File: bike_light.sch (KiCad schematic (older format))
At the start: 0 parts

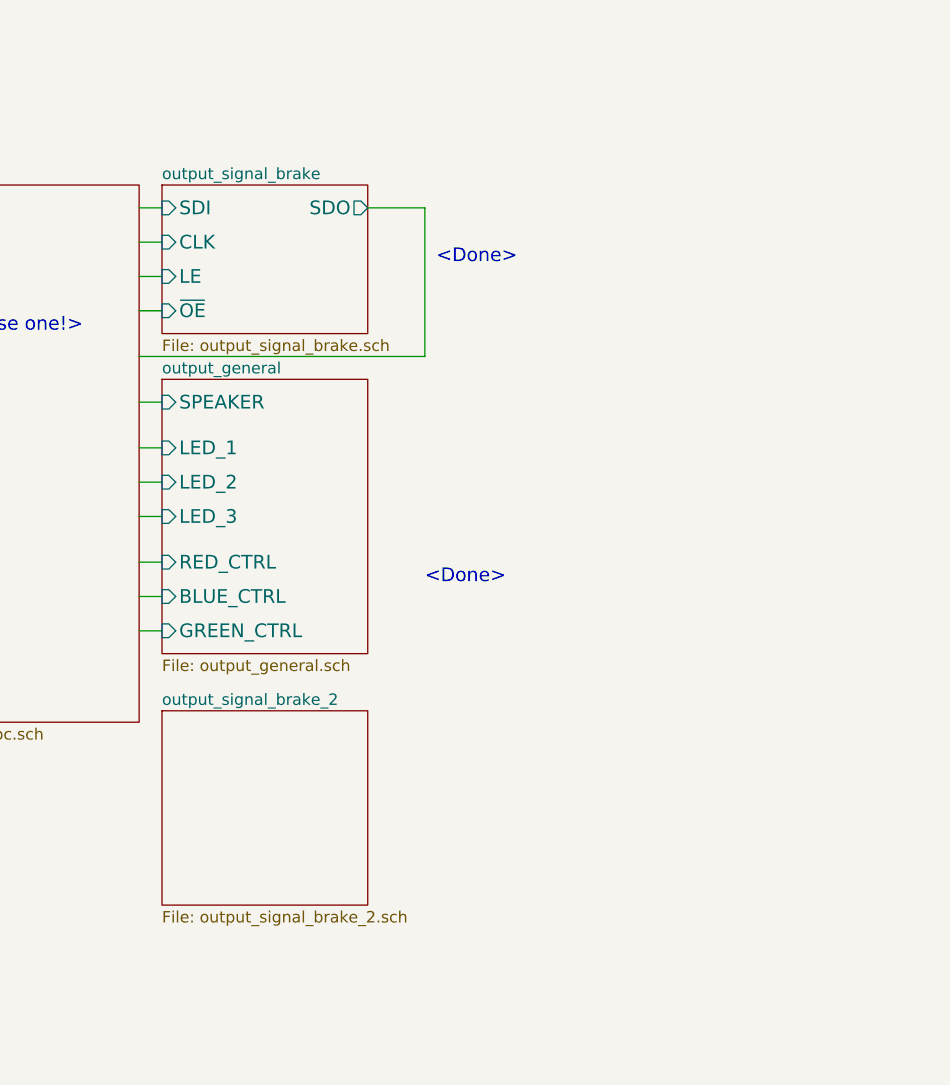
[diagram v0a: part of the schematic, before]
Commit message: finished batt-current LED driver array over I2C
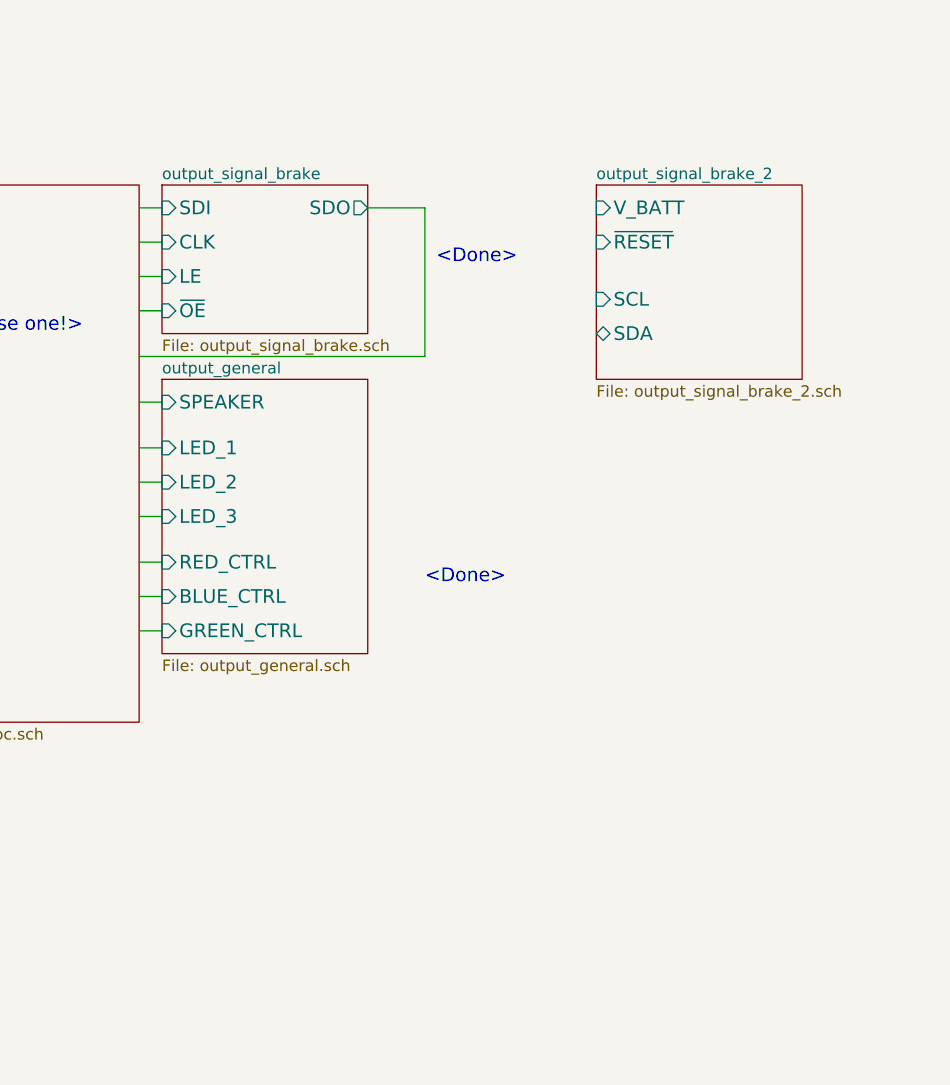
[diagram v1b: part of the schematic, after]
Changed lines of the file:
@@
 Sheet 1 16
 Title "Bike Light"
-Date "5 dec 2013"
+Date "6 dec 2013"
 Rev "1.0"
 Comp ""
@@
 $EndSheet
 $Sheet
-S 6700 4050 900  850
+S 8600 1750 900  850
 U 52A0B607
 F0 "output_signal_brake_2" 50
 F1 "output_signal_brake_2.sch" 50
+F2 "V_BATT" I L 8600 1850 60
+F3 "SCL" I L 8600 2250 60
+F4 "SDA" B L 8600 2400 60
+F5 "~RESET" I L 8600 2000 60
 $EndSheet
 $EndSCHEMATC

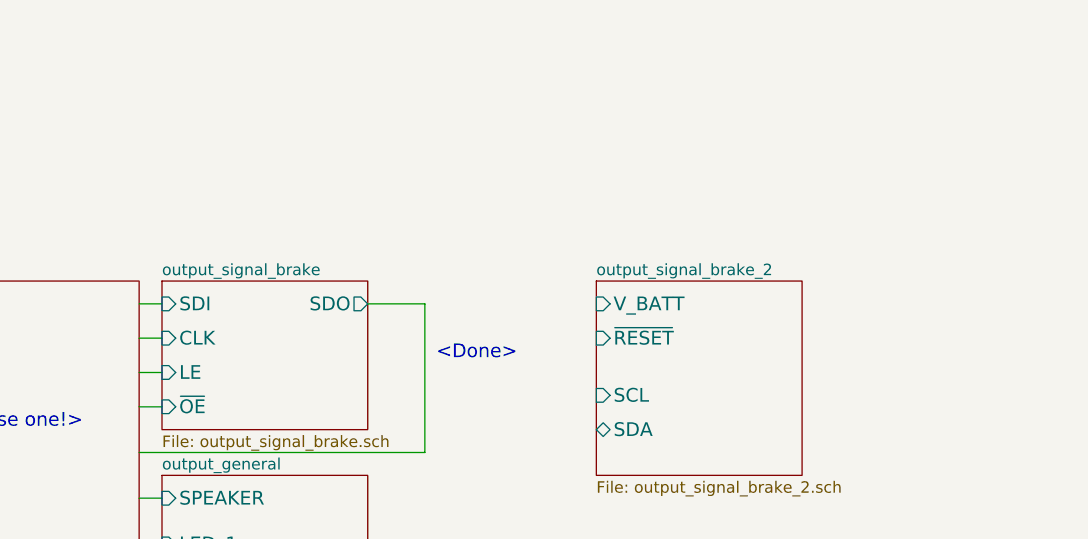
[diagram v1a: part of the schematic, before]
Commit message: added headlight sheet, led, dac
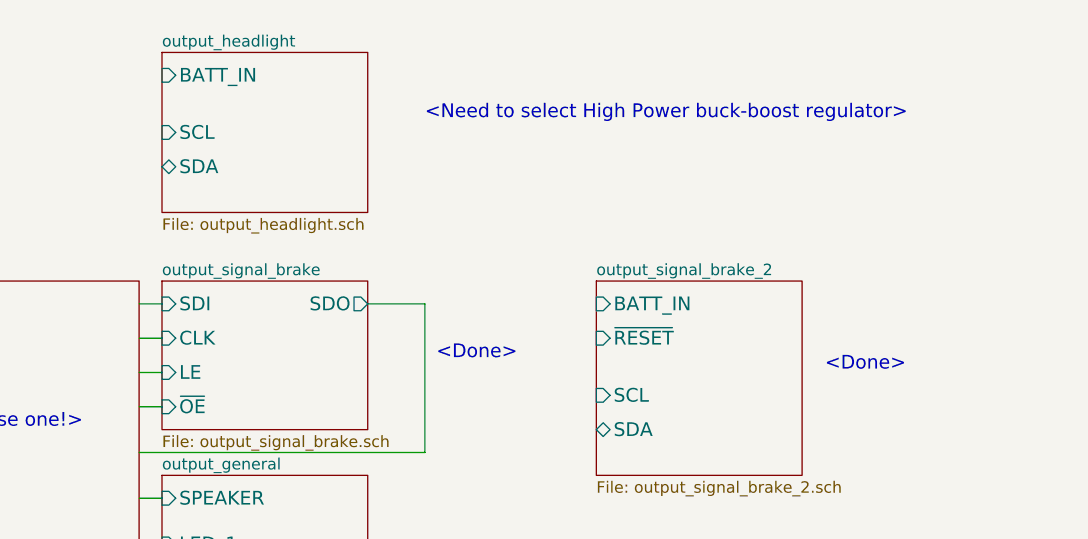
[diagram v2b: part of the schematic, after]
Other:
- note added: "<Need to select High Power buck-boost regulator>"
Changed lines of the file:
@@
 $Descr USLetter 11000 8500
 encoding utf-8
-Sheet 1 16
+Sheet 1 17
 Title "Bike Light"
-Date "6 dec 2013"
+Date "7 dec 2013"
 Rev "1.0"
 Comp ""
@@
 F0 "output_signal_brake_2" 50
 F1 "output_signal_brake_2.sch" 50
-F2 "V_BATT" I L 8600 1850 60
-F3 "SCL" I L 8600 2250 60
-F4 "SDA" B L 8600 2400 60
-F5 "~RESET" I L 8600 2000 60
-$EndSheet
+F2 "SCL" I L 8600 2250 60
+F3 "SDA" B L 8600 2400 60
+F4 "~RESET" I L 8600 2000 60
+F5 "BATT_IN" I L 8600 1850 60
+$EndSheet
+$Sheet
+S 6700 750  900  700
+U 52A3795F
+F0 "output_headlight" 50
+F1 "output_headlight.sch" 50
+F2 "SCL" I L 6700 1100 60
+F3 "SDA" B L 6700 1250 60
+F4 "BATT_IN" I L 6700 850 60
+$EndSheet
+Text Notes 9600 2150 0    60   ~ 0
+<Done>
+Text Notes 7850 1050 0    60   ~ 0
+<Need to select High Power buck-boost regulator>
 $EndSCHEMATC

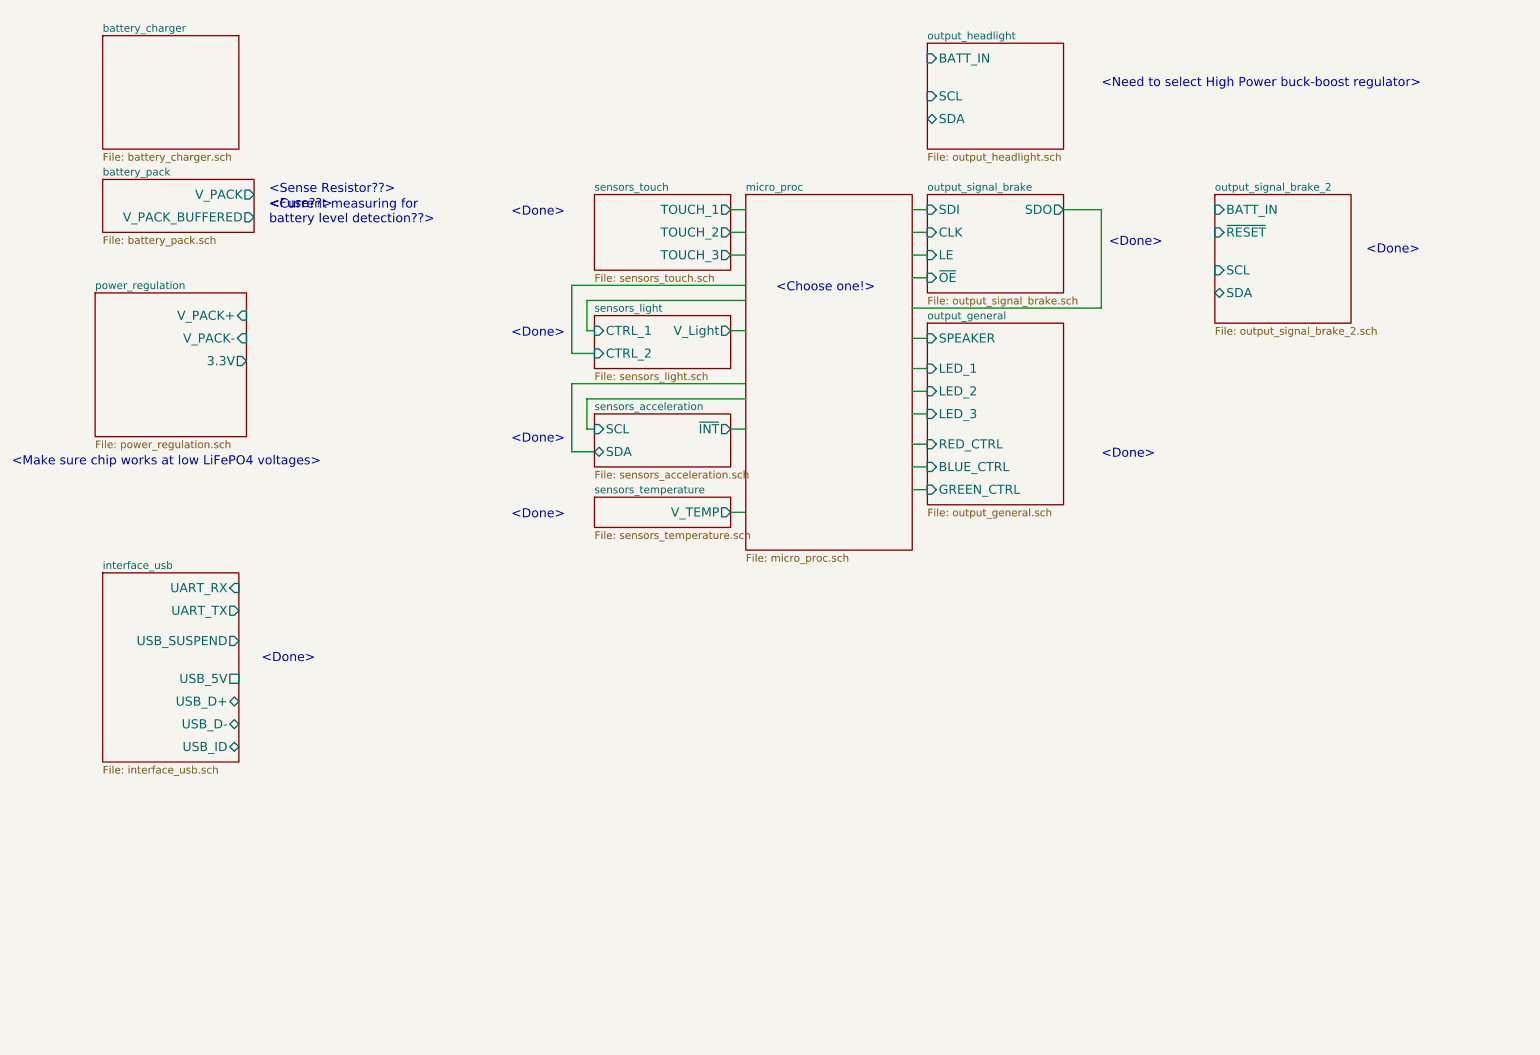
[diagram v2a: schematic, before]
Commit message: organized proc sheet I/O, organized I2C bus structure
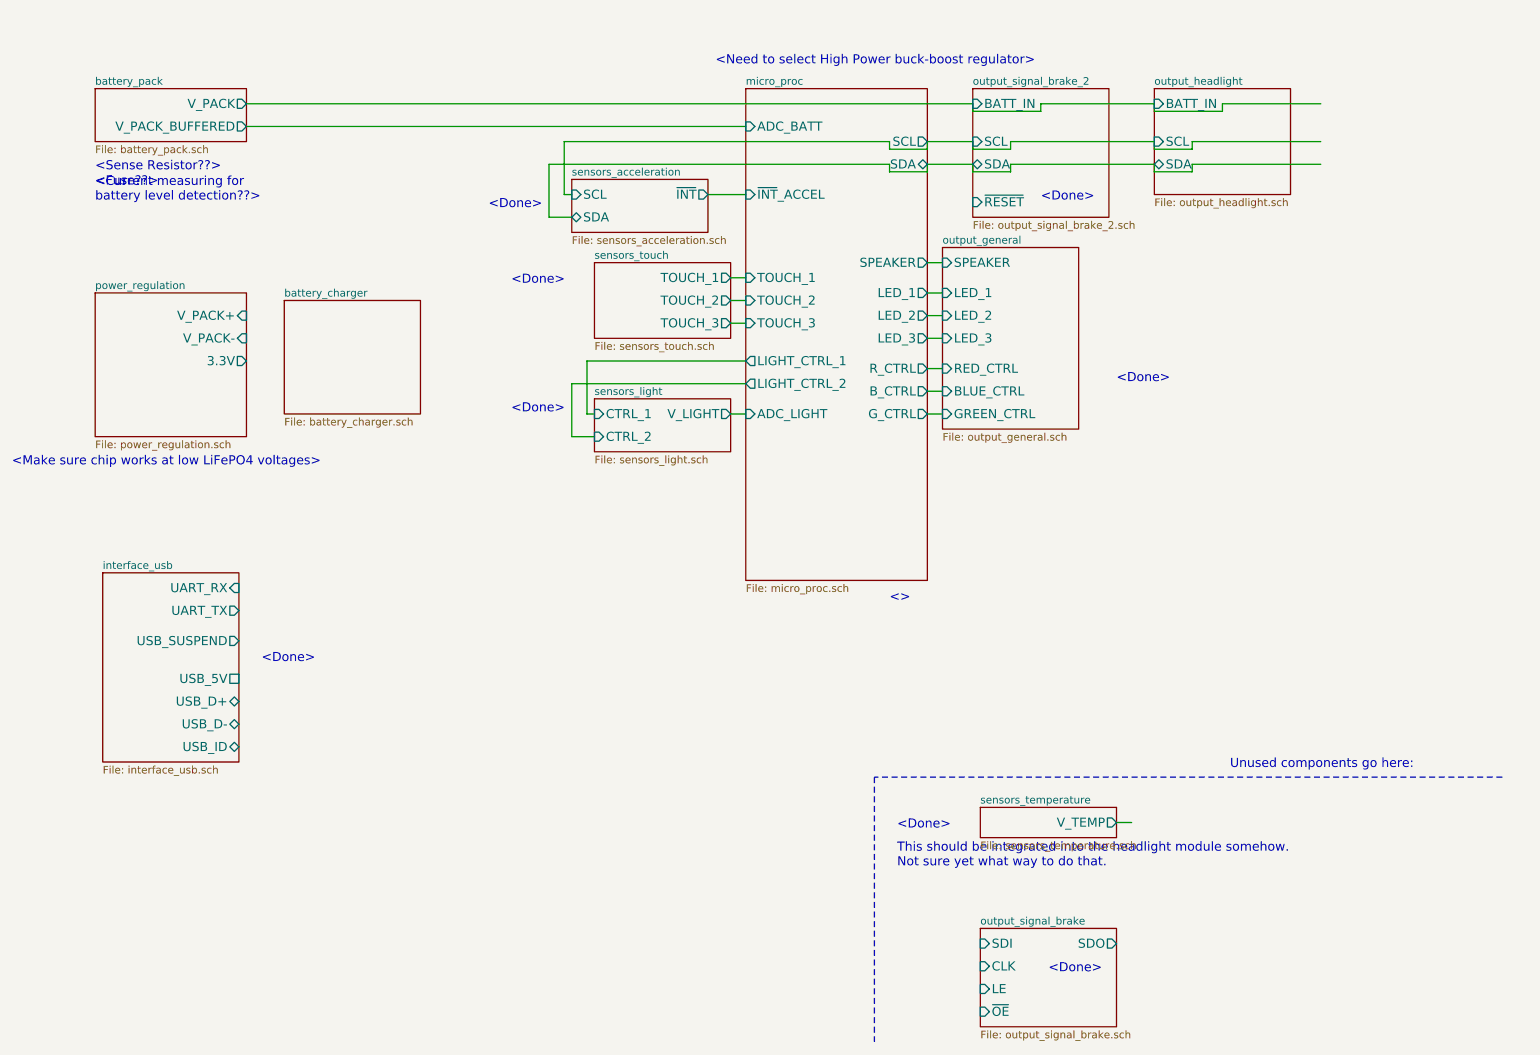
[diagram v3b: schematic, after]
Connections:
- wire segments 32 -> 59
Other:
- note added: "<>"
- note added: "This should be integrated into the headlight module somehow. \nNot sure yet what way to do that."
- note added: "Unused components go here:"
- note removed: "<Choose one!>"

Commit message: continued fleshing out proc
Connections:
- wire segments 59 -> 61
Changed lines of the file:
@@
 Sheet 1 17
 Title "Bike Light"
-Date "7 dec 2013"
+Date "8 dec 2013"
 Rev "1.0"
 Comp ""
@@
 F17 "LIGHT_CTRL_1" O L 5500 2850 60
 F18 "LIGHT_CTRL_2" O L 5500 3000 60
-$EndSheet
-$Sheet
-S 1250 4250 900  1250
+F19 "UART_RX" I L 5500 3900 60
+F20 "UART_TX" O L 5500 3750 60
+$EndSheet
+$Sheet
+S 4500 3650 900  1250
 U 5224C595
 F0 "interface_usb" 50
 F1 "interface_usb.sch" 50
-F2 "UART_RX" I R 2150 4350 60
-F3 "UART_TX" O R 2150 4500 60
-F4 "USB_SUSPEND" O R 2150 4700 60
-F5 "USB_5V" U R 2150 4950 60
-F6 "USB_D+" B R 2150 5100 60
-F7 "USB_D-" B R 2150 5250 60
-F8 "USB_ID" B R 2150 5400 60
+F2 "UART_RX" I R 5400 3750 60
+F3 "UART_TX" O R 5400 3900 60
+F4 "USB_SUSPEND" O R 5400 4100 60
+F5 "USB_5V" U R 5400 4350 60
+F6 "USB_D+" B R 5400 4500 60
+F7 "USB_D-" B R 5400 4650 60
+F8 "USB_ID" B R 5400 4800 60
 $EndSheet
 $Sheet
@@
 Text Notes 1200 1800 0    60   ~ 0
 <Current measuring for \nbattery level detection??>
-Text Notes 2300 4850 0    60   ~ 0
+Text Notes 5550 4250 0    60   ~ 0
 <Done>
 Text Notes 650  3550 0    60   ~ 0
@@
 Wire Wire Line
 	5400 3200 5500 3200
+Wire Wire Line
+	5500 3750 5400 3750
+Wire Wire Line
+	5400 3900 5500 3900
 $EndSCHEMATC
